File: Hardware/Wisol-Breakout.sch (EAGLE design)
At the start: 15 parts

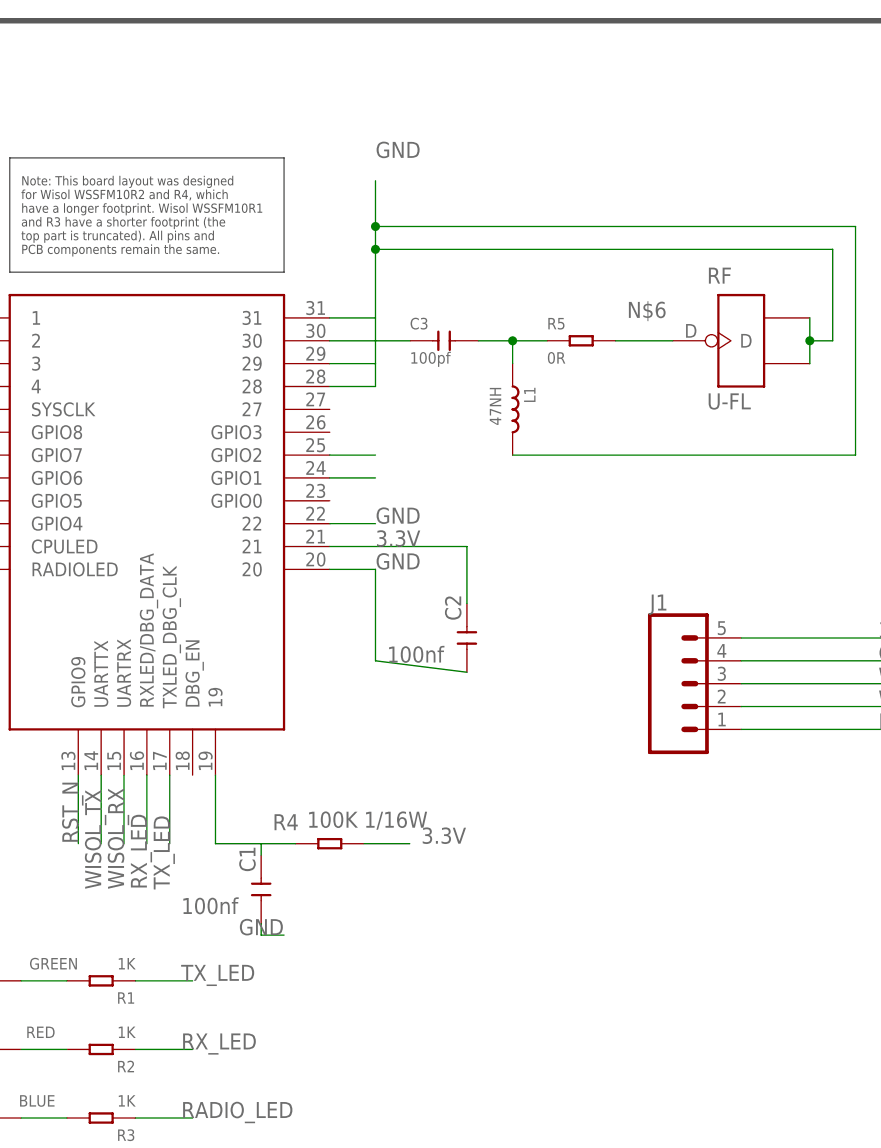
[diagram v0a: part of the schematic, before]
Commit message: Added annotations for Wisol WSSFM10R H/W Design Guide
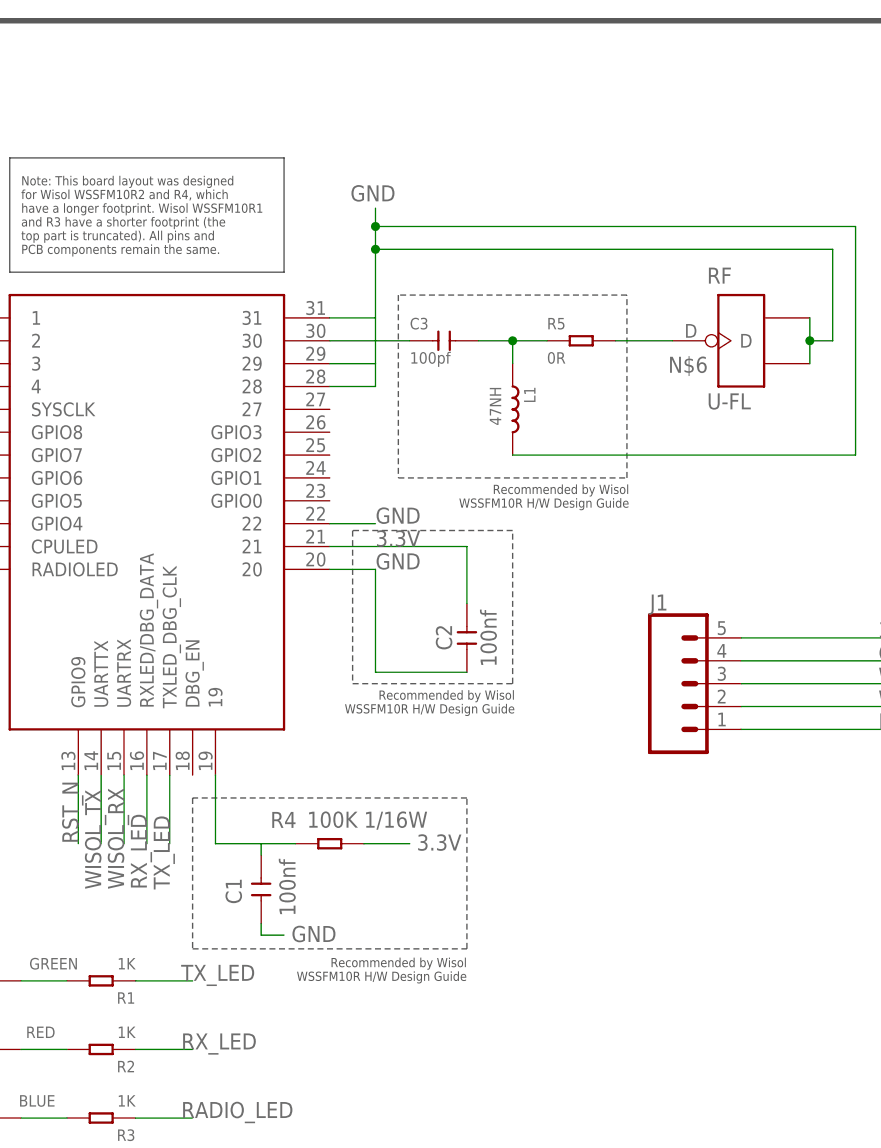
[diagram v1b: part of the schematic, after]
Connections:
- removed net GPIO1: WSSFM10R.GPIO1
- removed net GPIO2: WSSFM10R.GPIO2
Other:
- note added: "Recommended by Wisol WSSFM10R H/W Design Guide"
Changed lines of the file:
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@@
 top part is truncated). All pins and
 PCB components remain the same.</text>
+<wire x1="129.54" y1="132.08" x2="129.54" y2="111.76" width="0.1524" layer="97" style="longdash"/>
+<wire x1="129.54" y1="111.76" x2="154.94" y2="111.76" width="0.1524" layer="97" style="longdash"/>
+<wire x1="154.94" y1="111.76" x2="154.94" y2="132.08" width="0.1524" layer="97" style="longdash"/>
+<wire x1="154.94" y1="132.08" x2="129.54" y2="132.08" width="0.1524" layer="97" style="longdash"/>
+<text x="155.194" y="110.998" size="1.016" layer="97" align="top-right">Recommended by Wisol
+WSSFM10R H/W Design Guide</text>
+<wire x1="124.46" y1="105.918" x2="124.46" y2="88.9" width="0.1524" layer="97" style="longdash"/>
+<wire x1="124.46" y1="88.9" x2="142.24" y2="88.9" width="0.1524" layer="97" style="longdash"/>
+<wire x1="142.24" y1="88.9" x2="142.24" y2="105.918" width="0.1524" layer="97" style="longdash"/>
+<wire x1="142.24" y1="105.918" x2="124.46" y2="105.918" width="0.1524" layer="97" style="longdash"/>
+<wire x1="106.68" y1="76.2" x2="106.68" y2="59.436" width="0.1524" layer="97" style="longdash"/>
+<wire x1="106.68" y1="59.436" x2="137.16" y2="59.436" width="0.1524" layer="97" style="longdash"/>
+<wire x1="137.16" y1="59.436" x2="137.16" y2="76.2" width="0.1524" layer="97" style="longdash"/>
+<wire x1="137.16" y1="76.2" x2="106.68" y2="76.2" width="0.1524" layer="97" style="longdash"/>
+<text x="142.494" y="88.138" size="1.016" layer="97" align="top-right">Recommended by Wisol
+WSSFM10R H/W Design Guide</text>
+<text x="137.16" y="58.42" size="1.016" layer="97" align="top-right">Recommended by Wisol
+WSSFM10R H/W Design Guide</text>
 </plain>
 <instances>
@@
 <instance part="R3" gate="G$1" x="96.52" y="40.64" rot="R180"/>
 <instance part="R4" gate="G$1" x="121.92" y="71.12" smashed="yes">
-<attribute name="NAME" x="115.57" y="72.6186" size="1.778" layer="95"/>
+<attribute name="NAME" x="115.316" y="72.8726" size="1.778" layer="95"/>
 <attribute name="VALUE" x="119.38" y="72.898" size="1.778" layer="96"/>
 </instance>
 <instance part="C1" gate="G$1" x="114.3" y="66.04" smashed="yes" rot="R90">
-<attribute name="NAME" x="113.665" y="67.945" size="1.778" layer="95" rot="R90"/>
-<attribute name="VALUE" x="111.76" y="65.0875" size="1.778" layer="96" rot="R180"/>
+<attribute name="NAME" x="112.141" y="64.389" size="1.778" layer="95" rot="R90"/>
+<attribute name="VALUE" x="116.332" y="69.4055" size="1.778" layer="96" rot="R270"/>
 </instance>
 <instance part="C2" gate="G$1" x="137.16" y="93.98" smashed="yes" rot="R90">
-<attribute name="NAME" x="136.525" y="95.885" size="1.778" layer="95" rot="R90"/>
-<attribute name="VALUE" x="134.62" y="93.0275" size="1.778" layer="96" rot="R180"/>
+<attribute name="NAME" x="135.509" y="92.583" size="1.778" layer="95" rot="R90"/>
+<attribute name="VALUE" x="138.684" y="97.0915" size="1.778" layer="96" rot="R270"/>
 </instance>
 <instance part="J1" gate="G$1" x="160.02" y="88.9"/>
@@
 <wire x1="127" y1="121.92" x2="127" y2="124.46" width="0.1524" layer="91"/>
 <wire x1="127" y1="129.54" x2="127" y2="137.16" width="0.1524" layer="91"/>
-<label x="127" y="147.32" size="1.778" layer="95"/>
+<label x="124.206" y="142.494" size="1.778" layer="95"/>
 <pinref part="RF" gate="G$1" pin="GND1"/>
 <pinref part="RF" gate="G$1" pin="GND2"/>
 <wire x1="127" y1="137.16" x2="127" y2="139.7" width="0.1524" layer="91"/>
-<wire x1="127" y1="139.7" x2="127" y2="144.78" width="0.1524" layer="91"/>
+<wire x1="127" y1="139.7" x2="127" y2="141.732" width="0.1524" layer="91"/>
 <wire x1="175.26" y1="129.54" x2="175.26" y2="127" width="0.1524" layer="91"/>
 <wire x1="175.26" y1="127" x2="175.26" y2="124.46" width="0.1524" layer="91"/>
@@
 <label x="127" y="101.6" size="1.778" layer="95"/>
 <pinref part="C2" gate="G$1" pin="1"/>
-<wire x1="137.16" y1="90.17" x2="127" y2="91.44" width="0.1524" layer="91"/>
-<wire x1="127" y1="91.44" x2="127" y2="101.6" width="0.1524" layer="91"/>
+<wire x1="137.16" y1="90.17" x2="127" y2="90.17" width="0.1524" layer="91"/>
+<wire x1="127" y1="90.17" x2="127" y2="101.6" width="0.1524" layer="91"/>
 </segment>
 <segment>
@@
 <wire x1="114.3" y1="62.23" x2="114.3" y2="60.96" width="0.1524" layer="91"/>
 <wire x1="114.3" y1="60.96" x2="116.84" y2="60.96" width="0.1524" layer="91"/>
-<label x="116.84" y="60.96" size="1.778" layer="95" rot="MR0"/>
+<label x="122.682" y="60.198" size="1.778" layer="95" rot="MR0"/>
 </segment>
 <segment>
@@
 <pinref part="R4" gate="G$1" pin="2"/>
 <wire x1="125.73" y1="71.12" x2="130.81" y2="71.12" width="0.1524" layer="91"/>
-<label x="132.08" y="71.12" size="1.778" layer="95"/>
+<label x="131.572" y="70.358" size="1.778" layer="95"/>
 </segment>
 <segment>
@@
 </segment>
 </net>
-<net name="GPIO2" class="0">
-<segment>
-<pinref part="WSSFM10R" gate="G$1" pin="GPIO2"/>
-<wire x1="121.92" y1="114.3" x2="127" y2="114.3" width="0.1524" layer="91"/>
-</segment>
-</net>
-<net name="GPIO1" class="0">
-<segment>
-<pinref part="WSSFM10R" gate="G$1" pin="GPIO1"/>
-<wire x1="121.92" y1="111.76" x2="127" y2="111.76" width="0.1524" layer="91"/>
-</segment>
-</net>
 <net name="N$4" class="0">
 <segment>
@@
 <pinref part="R5" gate="G$1" pin="2"/>
 <wire x1="153.67" y1="127" x2="160.02" y2="127" width="0.1524" layer="91"/>
-<label x="154.94" y="129.54" size="1.778" layer="95"/>
-</segment>
-</net>
+<label x="159.512" y="123.444" size="1.778" layer="95"/>
+</segment>
+</net>
